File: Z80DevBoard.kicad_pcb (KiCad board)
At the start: 4 copper layers, 219 x 107.5 mm, 154 parts, among them J1 Conn_01x02_MountingPin, SW1 WAIT, SW2 RESET, SW3 Z80BOOT, SW4 RPBOOT, SW5 SW_Nidec_CAS-120A1, SW6 Z80_CLOCK, Y1 Crystal

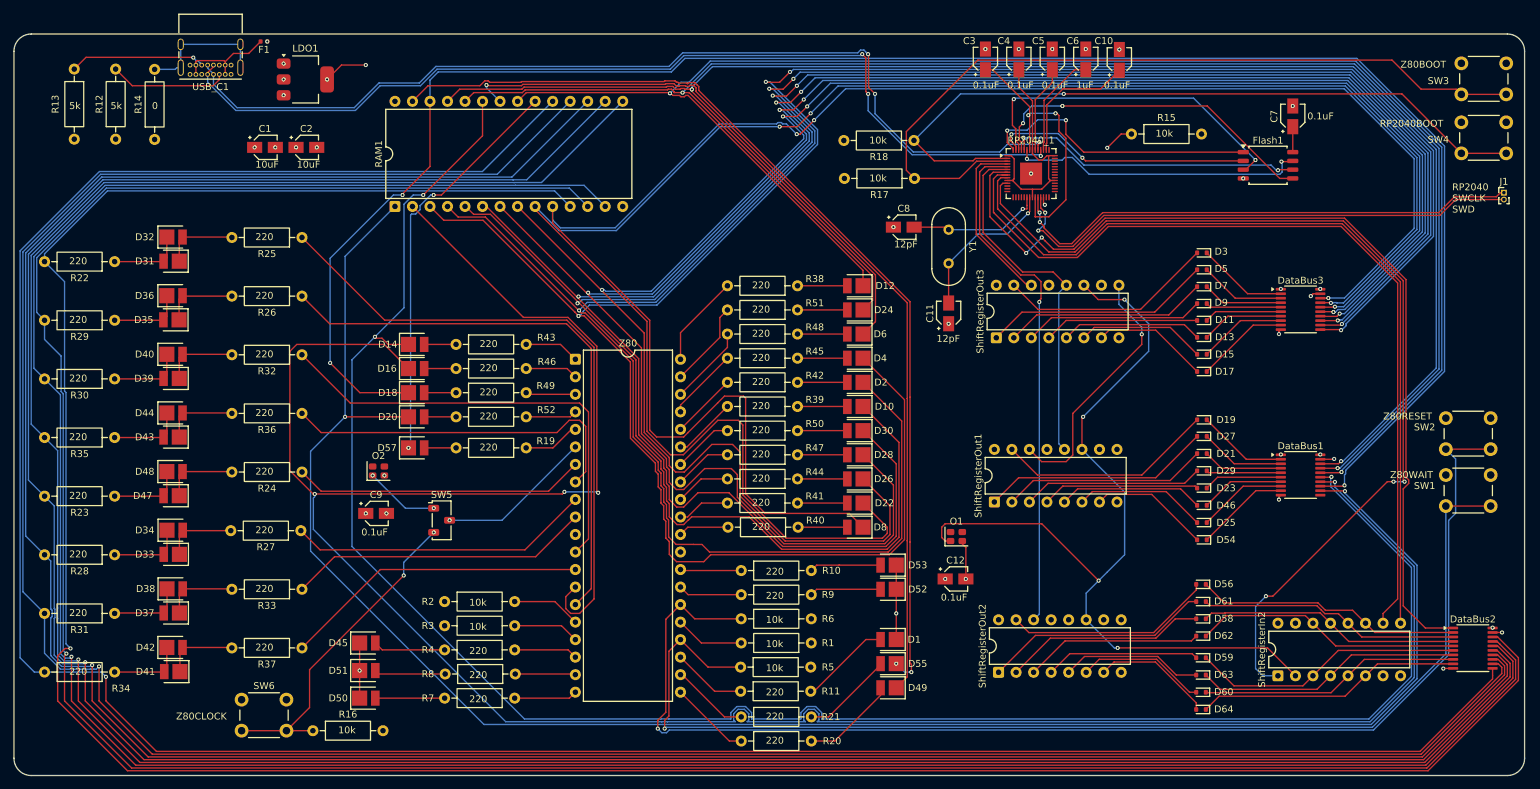
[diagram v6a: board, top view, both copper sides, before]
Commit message: Optimized the connections.
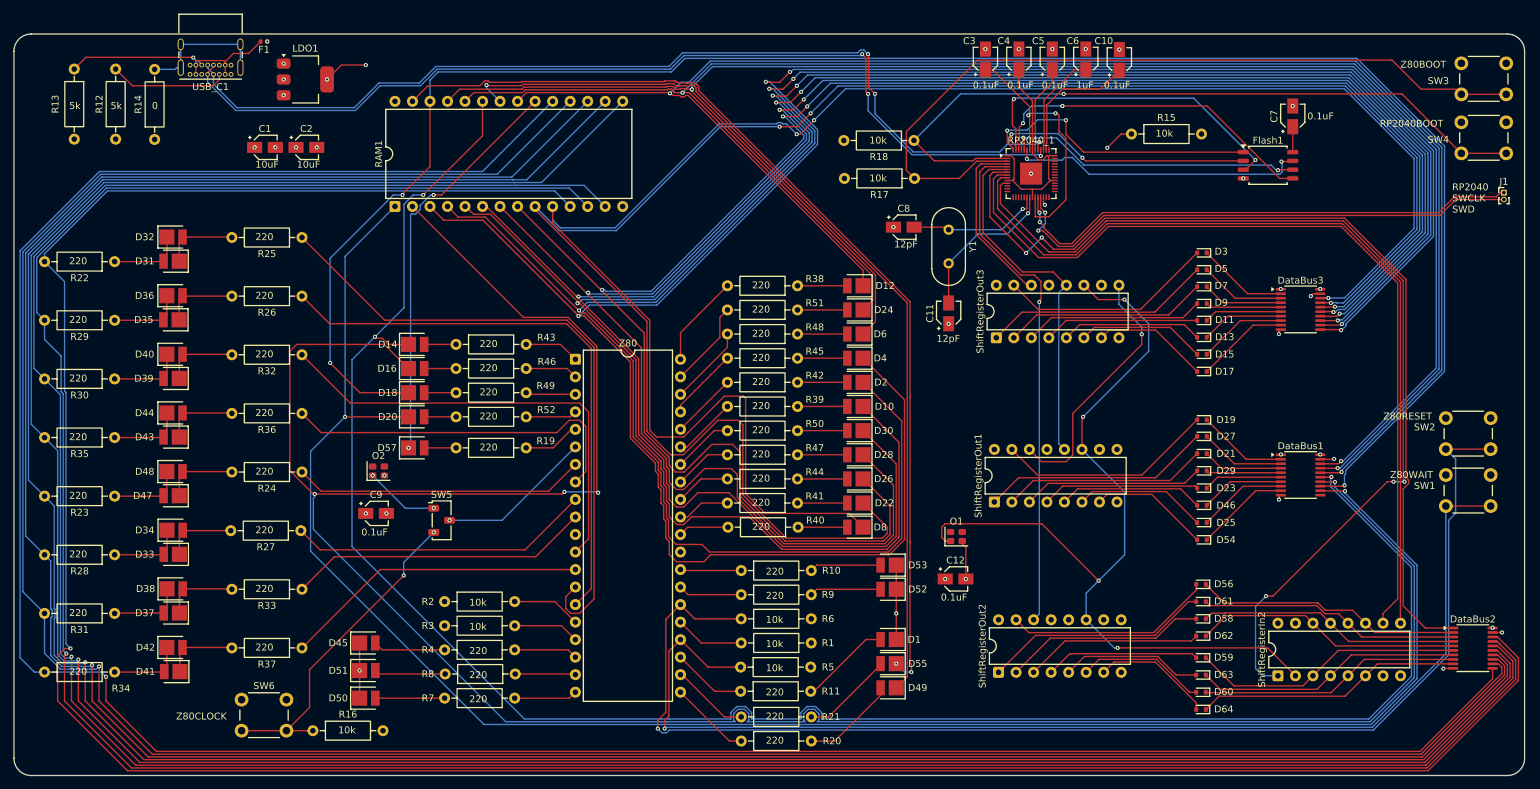
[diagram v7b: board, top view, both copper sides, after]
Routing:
- net GND: track 32.4 -> 30.3 mm
- net Net-(D52-A): track 11.6 -> 10.4 mm
- net Vcc: track 360.3 -> 359.2 mm
- net Net-(D55-A): track 14.2 -> 13.3 mm
- net Vdd_3v3: track 561.8 -> 561.0 mm
- net RP2040-RWRAM-GPIO6-DS: track 124.6 -> 123.9 mm
- net RAM-A5: track 304.3 -> 303.6 mm
- net Net-(D53-A): track 10.9 -> 10.4 mm

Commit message: Added the debouncer. Fixed the board sizes.
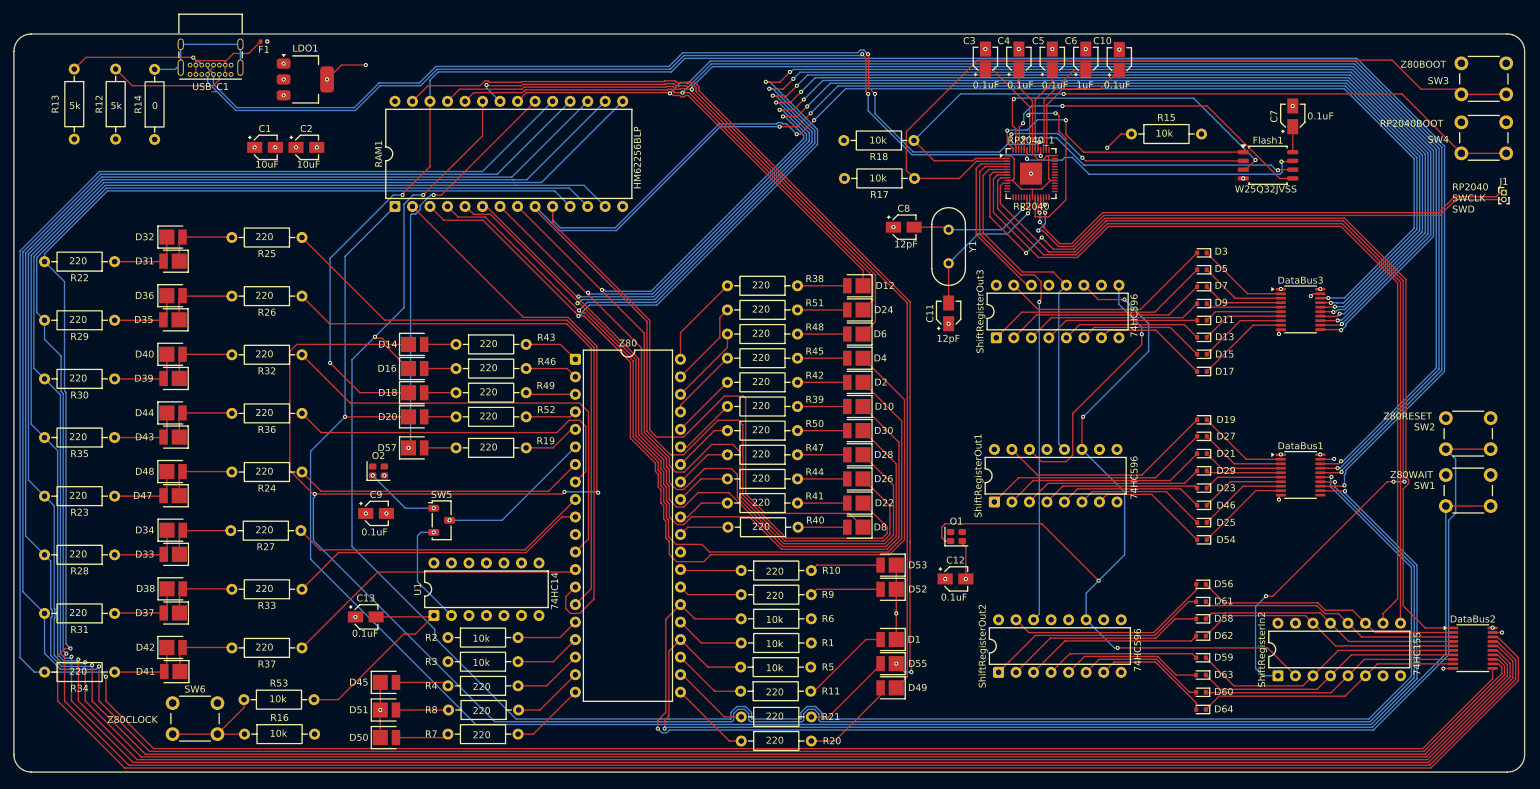
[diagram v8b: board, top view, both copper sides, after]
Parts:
- added C13: 0.1uF, Capacitor_SMD:CP_Elec_3x5.3, F.Cu at (89.0, 123.0)
- added R53: 10k, Resistor_THT:R_Axial_DIN0207_L6.3mm_D2.5mm_P10.16mm_Horizontal, F.Cu at (71.3, 135.0)
- added U1: 74HC14, Package_DIP:DIP-14_W7.62mm, F.Cu at (98.9, 122.8)
- moved SW6 10.0 mm to (61.0, 135.5)
- moved R16 9.93 mm to (71.4, 140.0)
- moved D50 6.45 mm to (92.0, 140.5)
- moved D51 6.45 mm to (92.0, 136.5)
- moved D45 6.45 mm to (92.0, 132.5)
- moved R7 5.24 mm to (111.1, 140.0)
- moved R8 5.24 mm to (111.2, 136.5)
- moved R2 5.24 mm to (100.9, 126.0)
- moved R3 5.24 mm to (111.1, 129.5)
- moved R4 5.24 mm to (111.1, 133.0)
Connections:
- R16 pad 1: Net-(SW5-A) -> Net-(R16-Pad1)
- R16 pad 2: GND -> Vdd_3v3
- SW5 pad 3: Net-(SW5-A) -> Z80_MANUAL_CLOCK
- SW6 pad 1: Vdd_3v3 -> GND
- SW6 pad 2: Net-(SW5-A) -> Net-(R16-Pad1)
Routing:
- net Net-(SW5-A): track 47.9 -> 0.00 mm, vias 2 -> 0
- net Net-(C13-Pad2): track 0.00 -> 30.9 mm
- net Net-(R16-Pad1): track 0.00 -> 17.0 mm
- net Z80_MANUAL_CLOCK: track 0.00 -> 16.2 mm, vias 0 -> 1
- net Vdd_3v3: track 561.0 -> 570.4 mm
- net Vcc: track 359.2 -> 365.6 mm
- net Net-(D51-A): track 10.3 -> 7.62 mm
- net Net-(D45-A): track 10.5 -> 7.75 mm
- net Net-(D50-A): track 10.0 -> 7.75 mm
- net Z80-MREQ: track 8.76 -> 10.5 mm
- net Z80-IORQ: track 9.16 -> 10.8 mm
- net RAM-A12: track 360.4 -> 359.4 mm
- net Z80-HALT: track 9.24 -> 10.0 mm
- net Z80-INT: track 10.0 -> 9.24 mm
- net RAM-A11: track 285.7 -> 286.4 mm
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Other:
- board size 219 x 107.5 mm -> 219 x 107 mm
- board text added: "74HC14"
- board text added: "74HC155"
- board text added: "74HC596"
- board text added: "HM62256BLP"
- board text added: "RP2040"
- board text added: "W25Q32JVSS"
